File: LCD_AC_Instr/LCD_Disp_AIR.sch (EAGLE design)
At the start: 12 parts, among them J1 CON_HEADER_1X02-PTH, SW1 ENCODER_SW1-PEC12

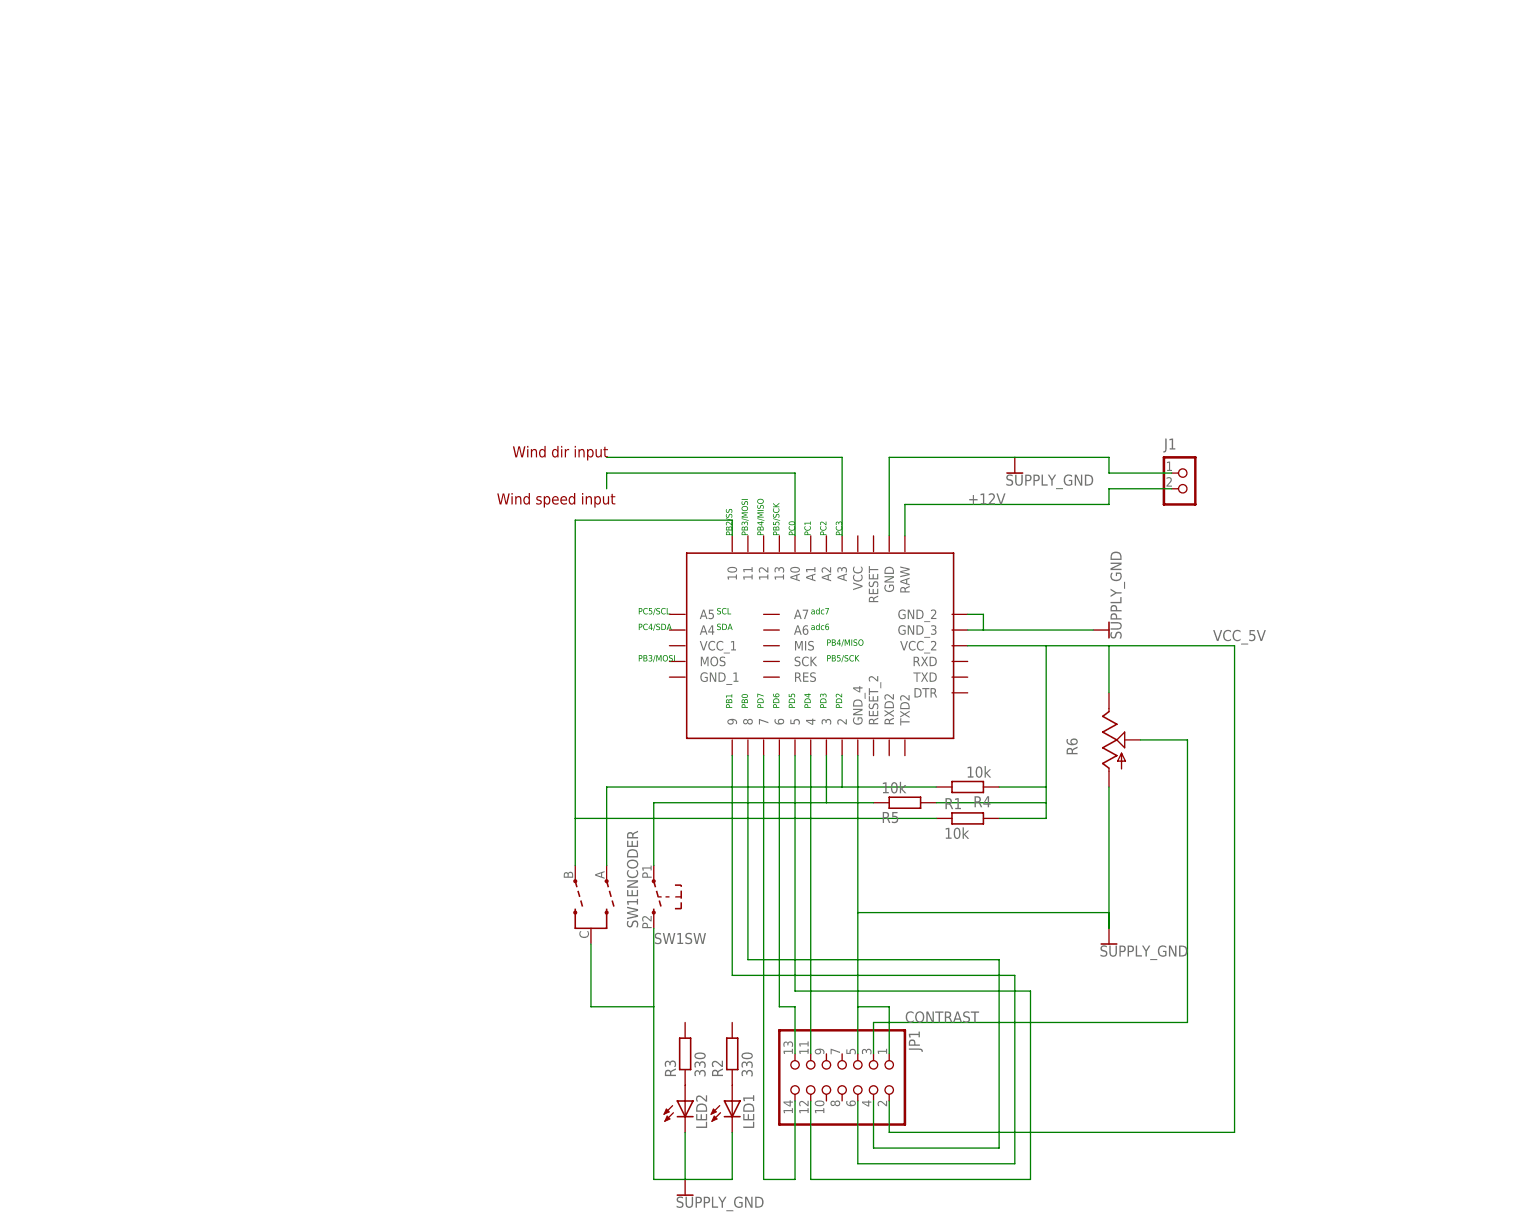
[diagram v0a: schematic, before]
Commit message: finished design of PCB and uploaded to OSH PCB
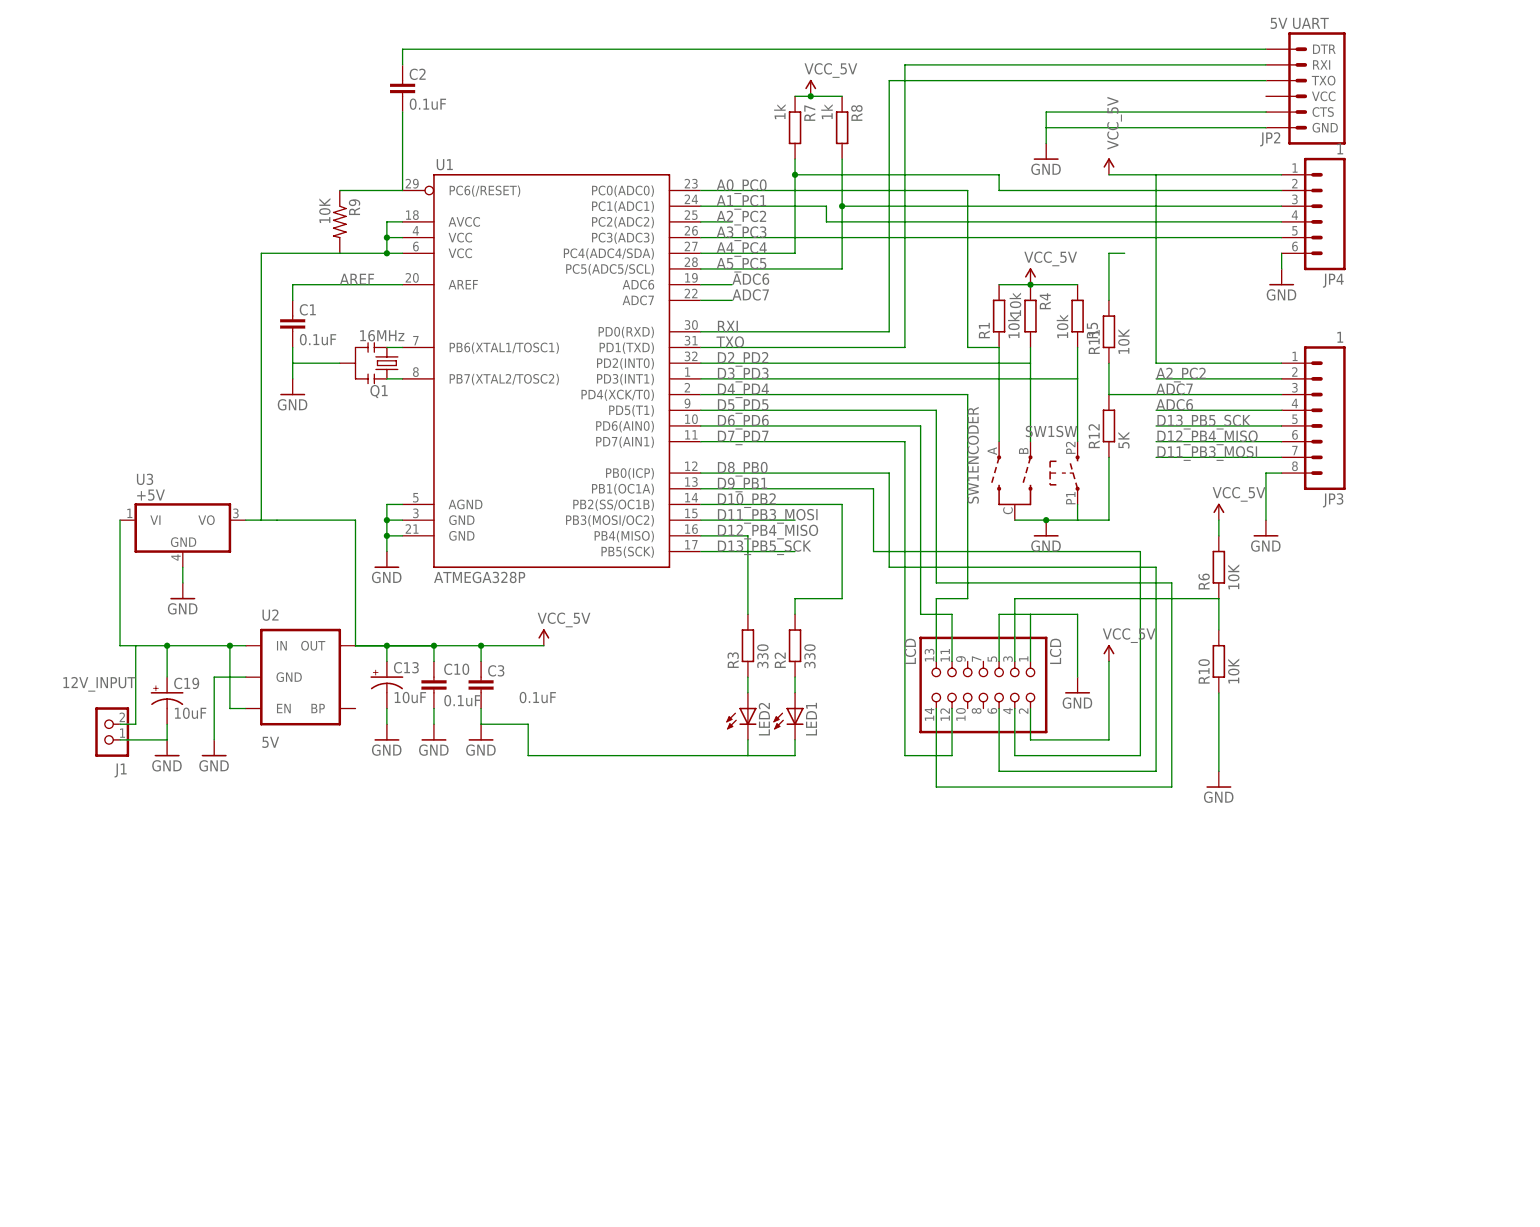
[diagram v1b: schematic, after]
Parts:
- removed JP1: (no value), pinhead:PINHD-2X7
- removed U$1: ARDUINO_PRO_MONI_DEEK_ROBOT, Arduino_Pro_FP:ARDUINO_PRO_MONI_DEEK_ROBOT
- added C1, C10, C2, C3: 0.1uF, SparkFun:CAP0402
- added C13, C19: 10uF, SparkFun:CAP_POL1206
- added JP2: 5V UART, SparkFun:ARDUINO_SERIAL_PROGRAMPTH
- added JP3: 1, SparkFun-Connectors:M081X08
- added JP4: 1, SparkFun-Connectors:M06SIP
- added LCD: LCD, pinhead:PINHD-2X7
- added Q1: 16MHz, SparkFun:RESONATORSMD
- added R10, R11: 10K, dp_devices:RESISTOR-0603
- added R12: 5K, dp_devices:RESISTOR-0603
- added R7, R8: 1k, dp_devices:RESISTOR-0603
- added R9: 10K, SparkFun:RESISTOR0402
- added U1: ATMEGA328P, SparkFun:ATMEGA168
- added U2: 5V, SparkFun:V_REG_LDOSMD
- added U3: +5V, wifi_WX:78MXXL
- J1: value CON_HEADER_1X02-PTH -> 12V input
- R6: value (none) -> 10K; device pot:TRIM_US-RJ6 -> dp_devices:RESISTOR-0603
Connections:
- removed net +12V: J1.2, U$1.RAW
- removed net CONTRAST: JP1.3, R6.S
- removed net N$1: JP1.11, U$1.4
- removed net N$10: R4.2, SW1ENCODER.A, U$1.2
- removed net N$11: U$1.A3
- removed net N$12: U$1.A0
- removed net N$3: JP1.12, U$1.5
- removed net N$4: JP1.6, U$1.9
- removed net N$7: R1.1, SW1ENCODER.B, U$1.10
- removed net VCC_5V: JP1.2, R1.2, R4.1, R5.2, R6.E, U$1.VCC_2
- new net 12V_INPUT: C19.+, J1.2, R11.2, U2.EN, U2.IN, U3.VI
- new net 5V: C10.1, C13.+, C3.2, JP3.1, JP4.1, LCD.2, R1.2, R4.1, R5.2, R6.2, R7.1, R8.1, R9.2, U1.AVCC, U1.VCC@1, U1.VCC@2, U2.OUT, U3.VO
- new net A0_PC0: R1.1, SW1ENCODER.A, U1.PC0(ADC0)
- new net A1_PC1: JP4.4, U1.PC1(ADC1)
- new net A2_PC2: JP3.2, U1.PC2(ADC2)
- new net A3_PC3: JP4.5, U1.PC3(ADC3)
- new net A4_PC4: JP4.2, R7.2, U1.PC4(ADC4/SDA)
- new net A5_PC5: JP4.3, R8.2, U1.PC5(ADC5/SCL)
- new net ADC6: JP3.4, U1.ADC6
- new net ADC7: JP3.3, R11.1, R12.2, U1.ADC7
- new net AREF: C1.2, U1.AREF
- new net D10_PB2: R2.2, U1.PB2(SS/OC1B)
- new net D11_PB3_MOSI: JP3.7, U1.PB3(MOSI/OC2)
- new net D12_PB4_MISO: JP3.6, R3.2, U1.PB4(MISO)
- new net D13_PB5_SCK: JP3.5, U1.PB5(SCK)
- new net D2_PD2: R4.2, SW1ENCODER.B, U1.PD2(INT0)
- new net D3_PD3: R5.1, SW1SW.2, U1.PD3(INT1)
- new net D4_PD4: LCD.13, U1.PD4(XCK/T0)
- new net D5_PD5: LCD.14, U1.PD5(T1)
- new net D6_PD6: LCD.11, U1.PD6(AIN0)
- new net D7_PD7: LCD.12, U1.PD7(AIN1)
- new net D8_PB0: LCD.6, U1.PB0(ICP)
- new net D9_PB1: LCD.4, U1.PB1(OC1A)
- new net RESET: C2.1, R9.1, U1.PC6(/RESET)
- new net RXI: JP2.TXO, U1.PD0(RXD)
- new net TXO: JP2.RXI, U1.PD1(TXD)
- net GND: now also C1.1, C10.2, C13.-, C19.-, C3.1, JP2.CTS, JP2.GND, JP3.8, JP4.6, LCD.1, LCD.5, Q1.2, R10.1, R12.1, SW1SW.1, U1.AGND, U1.GND@1, U1.GND@2, U2.GND, U3.GND; no longer JP1.1, JP1.5, R6.A, SW1SW.2, U$1.GND, U$1.GND_2, U$1.GND_3, U$1.GND_4
- net N$2: now also LCD.3, R10.2, R6.1; no longer JP1.13, U$1.6
- net N$5: now also Q1.1, U1.PB7(XTAL2/TOSC2); no longer JP1.4, U$1.8
- net N$6: now also C2.2, JP2.DTR; no longer R5.1, SW1SW.1, U$1.3
- net N$9: now also Q1.3, U1.PB6(XTAL1/TOSC1); no longer JP1.14, U$1.7
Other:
- note removed: "PB0"
- note removed: "PB1"
- note removed: "PB2/SS"
- note removed: "PB3/MOSI"
- note removed: "PB4/MISO"
- note removed: "PB5/SCK"
- note removed: "PC0"
- note removed: "PC1"
- note removed: "PC2"
- note removed: "PC3"
- note removed: "PC4/SDA"
- note removed: "PC5/SCL"
- note removed: "PD2"
- note removed: "PD3"
- note removed: "PD4"
- note removed: "PD5"
- note removed: "PD6"
- note removed: "PD7"
- note removed: "SCL"
- note removed: "SDA"
- note removed: "Wind dir input"
- note removed: "Wind speed input"
- note removed: "adc6"
- note removed: "adc7"
- moved on the sheet: J1, LED1, LED2, R1, R2, R3, R4, R5, SW1ENCODER, SW1SW

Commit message: labeled connectors
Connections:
- net A4_PC4 renamed A4_PC4_SDA
- net A5_PC5 renamed A5_PC5_SCL
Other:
- note added: "5V"
- note added: "A1"
- note added: "A2"
- note added: "A3"
- note added: "ADC6"
- note added: "ADC7"
- note added: "D11/MOSI"
- note added: "D12/MISO"
- note added: "D13/SCK"
- note added: "GND"
- note added: "SCL"
- note added: "SDA"
- moved on the sheet: R11, R12
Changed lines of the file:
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@@
 <sheet>
 <plain>
+<text x="200.66" y="190.5" size="1.778" layer="95">SDA</text>
+<text x="200.66" y="187.96" size="1.778" layer="95">SCL</text>
+<text x="200.66" y="182.88" size="1.778" layer="95">A3</text>
+<text x="200.66" y="185.42" size="1.778" layer="95">A1</text>
+<text x="200.66" y="193.04" size="1.778" layer="95">5V</text>
+<text x="200.66" y="162.56" size="1.778" layer="95">5V</text>
+<text x="200.66" y="144.78" size="1.778" layer="95">GND</text>
+<text x="200.66" y="180.34" size="1.778" layer="95">GND</text>
+<text x="200.66" y="160.02" size="1.778" layer="95">A2</text>
+<text x="200.66" y="157.48" size="1.778" layer="95">ADC7</text>
+<text x="200.66" y="154.94" size="1.778" layer="95">ADC6</text>
+<text x="200.66" y="152.4" size="1.778" layer="95">D13/SCK</text>
+<text x="200.66" y="149.86" size="1.778" layer="95">D12/MISO</text>
+<text x="200.66" y="147.32" size="1.778" layer="95">D11/MOSI</text>
 </plain>
 <instances>
@@
 <instance part="U3" gate="G$1" x="10.16" y="137.16"/>
 <instance part="GND2" gate="1" x="10.16" y="124.46"/>
-<instance part="R11" gate="G$1" x="160.02" y="167.64" rot="R90"/>
-<instance part="R12" gate="G$1" x="160.02" y="152.4" rot="R90"/>
+<instance part="R11" gate="G$1" x="162.56" y="167.64" rot="R90"/>
+<instance part="R12" gate="G$1" x="162.56" y="152.4" rot="R90"/>
 </instances>
 <busses>
@@
 <wire x1="154.94" y1="139.7" x2="154.94" y2="137.16" width="0.1524" layer="91"/>
 <pinref part="R12" gate="G$1" pin="1"/>
-<wire x1="160.02" y1="147.32" x2="160.02" y2="137.16" width="0.1524" layer="91"/>
-<wire x1="160.02" y1="137.16" x2="154.94" y2="137.16" width="0.1524" layer="91"/>
+<wire x1="162.56" y1="147.32" x2="162.56" y2="137.16" width="0.1524" layer="91"/>
+<wire x1="162.56" y1="137.16" x2="154.94" y2="137.16" width="0.1524" layer="91"/>
 </segment>
 <segment>
@@
 </segment>
 </net>
-<net name="A5_PC5" class="0">
+<net name="A5_PC5_SCL" class="0">
 <segment>
 <label x="96.52" y="177.8" size="1.778" layer="95"/>
@@
 </segment>
 </net>
-<net name="A4_PC4" class="0">
+<net name="A4_PC4_SDA" class="0">
 <segment>
 <wire x1="93.98" y1="180.34" x2="109.22" y2="180.34" width="0.1524" layer="91"/>
@@
 <segment>
 <pinref part="R11" gate="G$1" pin="2"/>
-<wire x1="160.02" y1="172.72" x2="160.02" y2="180.34" width="0.1524" layer="91"/>
-<wire x1="160.02" y1="180.34" x2="162.56" y2="180.34" width="0.1524" layer="91"/>
+<wire x1="162.56" y1="172.72" x2="162.56" y2="180.34" width="0.1524" layer="91"/>
+<wire x1="162.56" y1="180.34" x2="165.1" y2="180.34" width="0.1524" layer="91"/>
+<label x="167.64" y="180.34" size="1.778" layer="95"/>
 </segment>
 </net>
@@
 </segment>
 <segment>
-<wire x1="187.96" y1="157.48" x2="160.02" y2="157.48" width="0.1524" layer="91"/>
+<wire x1="187.96" y1="157.48" x2="162.56" y2="157.48" width="0.1524" layer="91"/>
 <label x="167.64" y="157.48" size="1.778" layer="95"/>
 <pinref part="JP3" gate="G$1" pin="3"/>
 <pinref part="R12" gate="G$1" pin="2"/>
 <pinref part="R11" gate="G$1" pin="1"/>
-<wire x1="160.02" y1="162.56" x2="160.02" y2="157.48" width="0.1524" layer="91"/>
-</segment>
-</net>
+<wire x1="162.56" y1="162.56" x2="162.56" y2="157.48" width="0.1524" layer="91"/>
+</segment>
+</net>

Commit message: Revised to rev 0.1
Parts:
- removed U2: 5V, SparkFun:V_REG_LDOSMD
- added C4, C5, C6, C8, C9: 0.1uF, SparkFun:CAP0805
- added C7: 10uF, SparkFun:CAP_POL1206
- added F1: (no value), dp_devices:FUSE_PTC-0805
- added IC3: TC10553.3V, 1AA_Stofer:TC10553.3V
- C1, C10, C2, C3: device SparkFun:CAP0402 -> SparkFun:CAP0805
- C19: device SparkFun:CAP_POL1206 -> SparkFun:CAP_POL7343
- R10: value 10K -> 120
- R11: value 10K -> 14K
- R12: value 5K -> 6.8K
- R2, R3: value 330 -> 470
- R6: value 10K -> (none)
- R9: device SparkFun:RESISTOR0402 -> SparkFun:RESISTOR0603
- U1: value ATMEGA328P -> ATMEGA328P-AU(R)
- U3: value +5V -> 78M05
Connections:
- removed net D2_PD2: R4.2, SW1ENCODER.B, U1.PD2(INT0)
- removed net D3_PD3: R5.1, SW1SW.2, U1.PD3(INT1)
- new net D2_PD2(INT0): C4.2, R1.1, SW1ENCODER.A, U1.PD2(INT0)
- new net D3_PD3(INT1): C6.2, R5.1, SW1SW.1, U1.PD3(INT1)
- new net N$11: F1.1, J1.2
- new net V3_3V: C7.+, C8.1, IC3.OUT, JP4.5
- net 12V_INPUT: now also F1.2; no longer J1.2, U2.EN, U2.IN
- net 5V: now also IC3.EN, IC3.IN; no longer U2.OUT
- net A0_PC0: now also C5.2, R4.2, SW1ENCODER.B; no longer R1.1, SW1ENCODER.A
- net A3_PC3: now also R3.2; no longer JP4.5
- net ADC7: now also C9.1; no longer JP3.3
- net D12_PB4_MISO: no longer R3.2
- net GND: now also C4.1, C5.1, C6.1, C7.-, C8.2, C9.2, IC3.GND, SW1SW.2; no longer SW1SW.1, U2.GND
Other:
- note added: "Add C4,C5,C6,C7,C8 (air)"
- note added: "Cut and jumper JP4(5) to V3_3V"
- note added: "Cut and jumper R3 to PC3,A3"
- note added: "For rev 0.0 artwork:"
- note added: "Or LP3990"
- note removed: "A3"
- note removed: "ADC7"
- moved on the sheet: C1, C19, C2, J1, JP2, JP3, JP4, LED1, LED2, Q1, R10, R11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
